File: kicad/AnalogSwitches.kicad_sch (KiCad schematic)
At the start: 63 parts

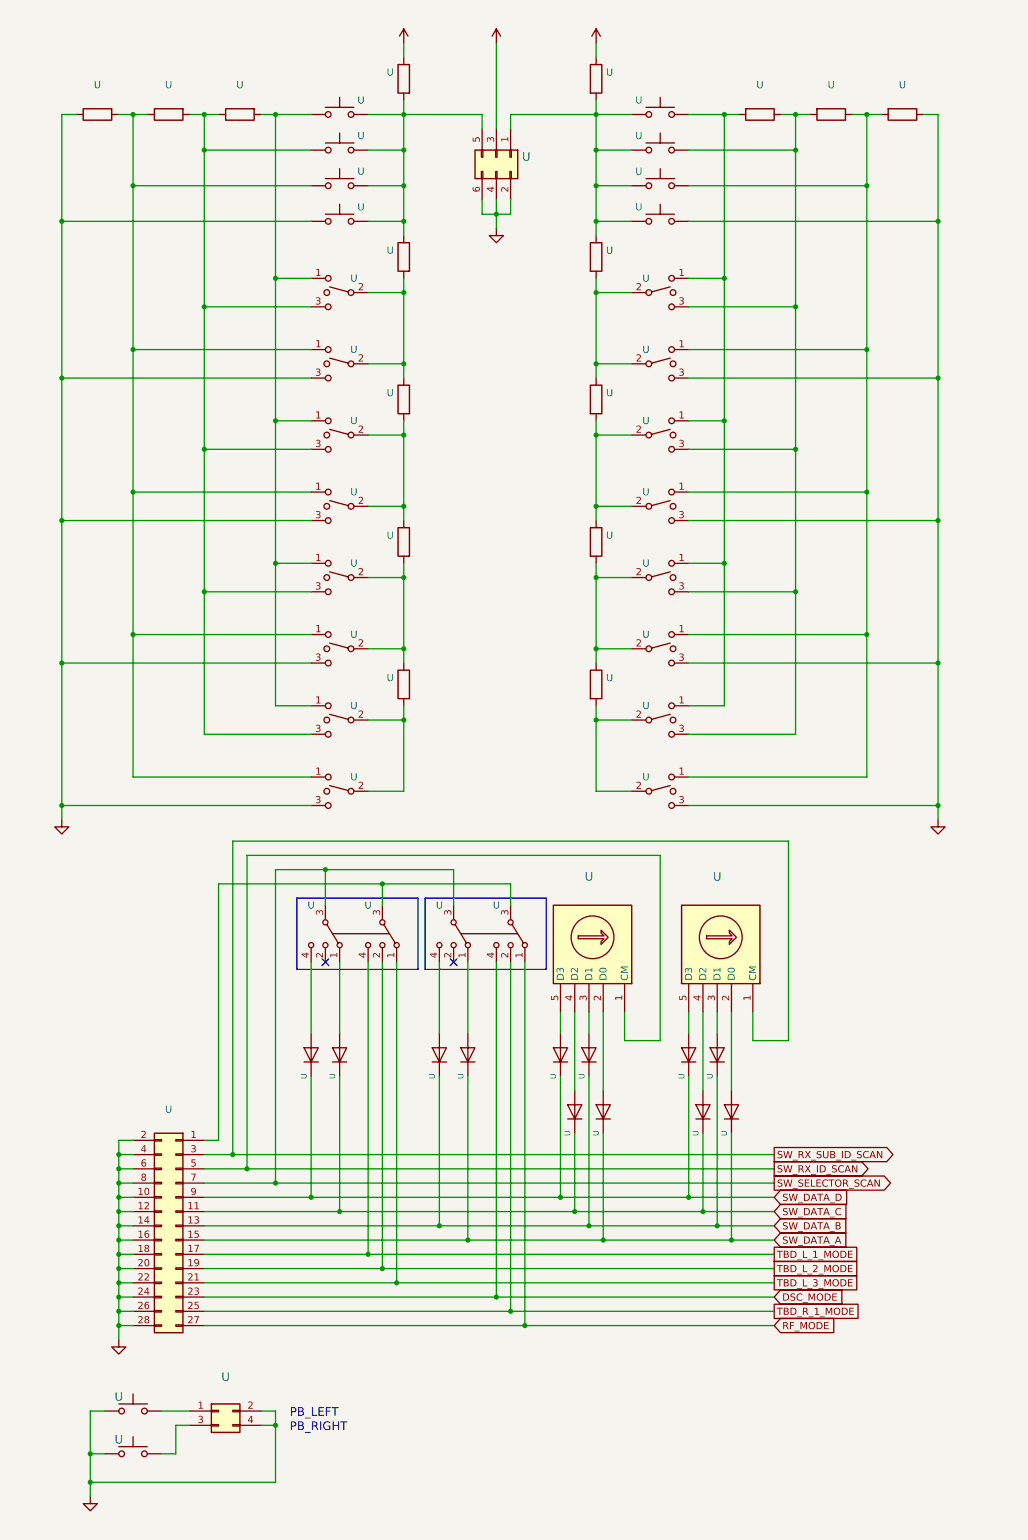
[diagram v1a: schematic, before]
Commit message: Adding PIB USB BRIDGE UML state diagrams - WIP
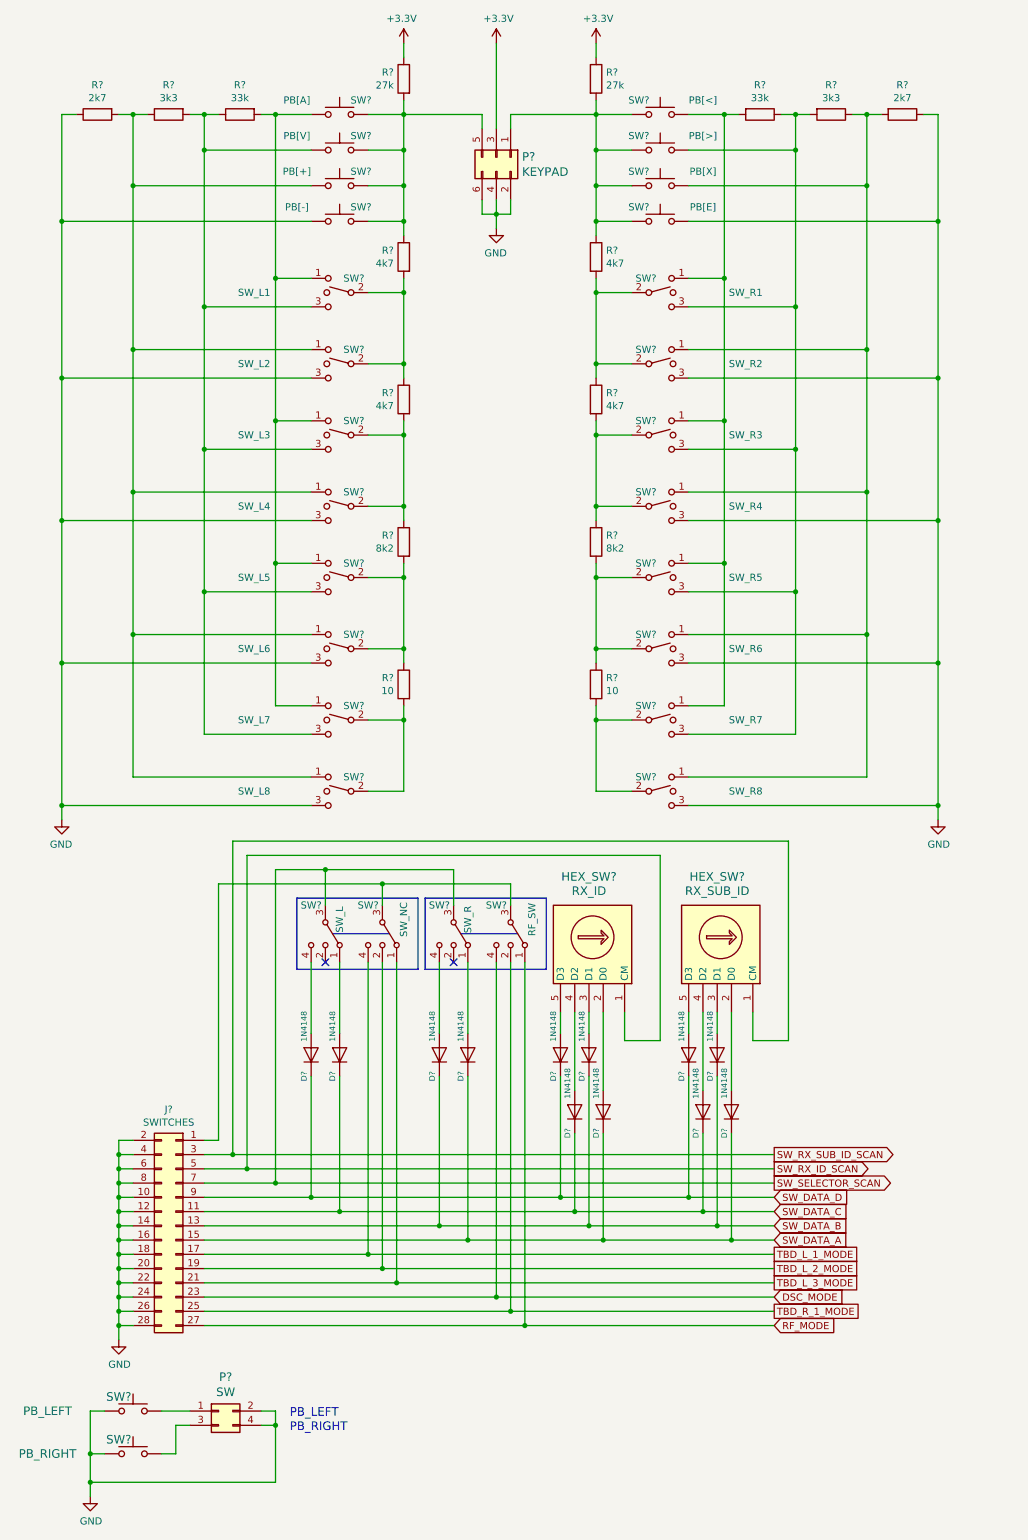
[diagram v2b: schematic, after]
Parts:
- D? (x12): renamed from U; value (none) -> 1N4148; footprint (none) -> Diodes_THT:D_5W_P5.08mm_Vertical_KathodeUp
- HEX_SW?: renamed from U; value (none) -> RX_SUB_ID; footprint (none) -> Buttons_Switches_THT:Nidec_Copal_SH-7010C
- HEX_SW?: renamed from U; value (none) -> RX_ID; footprint (none) -> Buttons_Switches_THT:Nidec_Copal_SH-7010C
- J?: renamed from U; value (none) -> SWITCHES
- P?: renamed from U; value (none) -> KEYPAD
- P?: renamed from U; value (none) -> SW
- R? (x4): renamed from U; value (none) -> 4k7
- R? (x2): renamed from U; value (none) -> 8k2
- R? (x2): renamed from U; value (none) -> 10
- R? (x2): renamed from U; value (none) -> 27k
- R? (x2): renamed from U; value (none) -> 33k
- R? (x2): renamed from U; value (none) -> 3k3
- R? (x2): renamed from U; value (none) -> 2k7
- SW?: renamed from U; value (none) -> SW_L1
- SW?: renamed from U; value (none) -> SW_L2
- SW?: renamed from U; value (none) -> SW_L3
- SW?: renamed from U; value (none) -> SW_L4
- SW?: renamed from U; value (none) -> SW_L5
- SW?: renamed from U; value (none) -> SW_L6
- SW?: renamed from U; value (none) -> SW_L7
- SW?: renamed from U; value (none) -> SW_L8
- SW?: renamed from U; value (none) -> PB[A]
- SW?: renamed from U; value (none) -> PB[V]
- SW?: renamed from U; value (none) -> SW_R1
- SW?: renamed from U; value (none) -> SW_R2
- SW?: renamed from U; value (none) -> SW_R3
- SW?: renamed from U; value (none) -> SW_R4
- SW?: renamed from U; value (none) -> SW_R5
- SW?: renamed from U; value (none) -> SW_R6
- SW?: renamed from U; value (none) -> SW_R7
- SW?: renamed from U; value (none) -> SW_R8
- SW?: renamed from U; value (none) -> PB[<]
- SW?: renamed from U; value (none) -> RF_SW; footprint (none) -> Buttons_Switches_THT:SW_CuK_JS202011AQN_DPDT_Angled
- SW?: renamed from U; value (none) -> SW_R; footprint (none) -> Buttons_Switches_THT:SW_CuK_JS202011AQN_DPDT_Angled
- SW?: renamed from U; value (none) -> SW_NC; footprint (none) -> Buttons_Switches_THT:SW_CuK_JS202011AQN_DPDT_Angled
- SW?: renamed from U; value (none) -> SW_L; footprint (none) -> Buttons_Switches_THT:SW_CuK_JS202011AQN_DPDT_Angled
- SW?: renamed from U; value (none) -> PB[+]
- SW?: renamed from U; value (none) -> PB[-]
- SW?: renamed from U; value (none) -> PB[>]
- SW?: renamed from U; value (none) -> PB[X]
- SW?: renamed from U; value (none) -> PB[E]
- SW?: renamed from U; value (none) -> PB_LEFT
- SW?: renamed from U; value (none) -> PB_RIGHT

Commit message: Optimizing power lines
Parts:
- removed J?: SWITCHES, symbol conn:Conn_02x14_Odd_Even
- added D38, D39, D40, D41: 1N4148, Diodes_THT:D_5W_P5.08mm_Vertical_KathodeUp, symbol RCTX-rescue:D-device
- added HEX_SW1: RF_BAND_SEL, Buttons_Switches_THT:Nidec_Copal_SH-7010C, symbol RCTX-rescue:SW_Coded-switches
- added J?: SWITCHES, symbol Connector_Generic:Conn_02x15_Odd_Even
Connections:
- net DSC_MODE: now also J?.25 (Pin_25)
- net GND: now also J?.10 (Pin_10), J?.12 (Pin_12), J?.14 (Pin_14), J?.16 (Pin_16), J?.18 (Pin_18), J?.2 (Pin_2), J?.20 (Pin_20), J?.22 (Pin_22), J?.24 (Pin_24), J?.26 (Pin_26), J?.28 (Pin_28), J?.30 (Pin_30), J?.4 (Pin_4), J?.6 (Pin_6), J?.8 (Pin_8)
- net RF_MODE: now also J?.29 (Pin_29)
- net SW_DATA_A: now also D41.1 (K), J?.17 (Pin_17)
- net SW_DATA_B: now also D40.1 (K), J?.15 (Pin_15)
- net SW_DATA_C: now also D39.1 (K), J?.13 (Pin_13)
- net SW_DATA_D: now also D38.1 (K), J?.11 (Pin_11)
- net SW_RX_ID_SCAN: now also J?.5 (Pin_5)
- net SW_RX_SUB_ID_SCAN: now also J?.7 (Pin_7)
- net SW_SELECTOR_SCAN: now also J?.9 (Pin_9)
- net TBD_L_1_MODE: now also J?.19 (Pin_19)
- net TBD_L_2_MODE: now also J?.21 (Pin_21)
- net TBD_L_3_MODE: now also J?.23 (Pin_23)
- net TBD_R_1_MODE: now also J?.27 (Pin_27)
- net at SW?.3, SW?.3: now also J?.1 (Pin_1)
- new net: D41.2 (A), HEX_SW1.2 (D0)
- new net: D38.2 (A), HEX_SW1.5 (D3)
- new net: D39.2 (A), HEX_SW1.4 (D2)
- new net: D40.2 (A), HEX_SW1.3 (D1)
- new net SW_RF_BAND_SCAN: HEX_SW1.1 (CM), J?.3 (Pin_3)
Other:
- moved on the sheet: D?, HEX_SW?, SW?
